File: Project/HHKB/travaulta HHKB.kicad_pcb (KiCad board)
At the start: 4 copper layers, 209.7 x 76.4 mm, 107 parts, among them J1 ARGB, SW1 EC_SW, SW10 EC_SW, SW11 EC_SW, SW12 EC_SW, SW13 EC_SW, SW14 EC_SW, SW15 EC_SW, SW16 EC_SW, SW17 EC_SW, SW18 EC_SW, SW19 EC_SW, SW2 EC_SW, SW20 EC_SW, SW21 EC_SW, SW22 EC_SW, SW23 EC_SW, SW24 EC_SW, SW25 EC_SW, SW26 EC_SW, SW27 EC_SW, SW28 EC_SW, SW29 EC_SW, SW3 EC_SW, SW30 EC_SW, SW31 EC_SW, SW32 EC_SW, SW33 EC_SW, SW34 EC_SW, SW35 EC_SW, SW36 EC_SW, SW37 EC_SW, SW38 BOOT0, SW4 EC_SW, SW5 EC_SW, SW6 EC_SW, SW7 EC_SW, SW8 EC_SW, SW9 EC_SW, U1 STM32F401CBUx, U2 XC6206PxxxMR, U3 74HC4051, U4 74HC4051, U5 OPA350, Y1 8 MHz

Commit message: backup
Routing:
- net GND: track 37.7 -> 45.2 mm, vias 325 -> 321
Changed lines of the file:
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@@
   (via (at 195.012249 65.997905) (size 0.8) (drill 0.4) (layers "F.Cu" "B.Cu") (free) (net 1))
   (via (at 120.888576 104.225245) (size 0.8) (drill 0.4) (layers "F.Cu" "B.Cu") (free) (net 1))
-  (via (at 153.288724 110.807639) (size 0.8) (drill 0.4) (layers "F.Cu" "B.Cu") (net 1))
   (via (at 63.221009 85.070745) (size 0.8) (drill 0.4) (layers "F.Cu" "B.Cu") (free) (net 1))
   (via (at 211.90546 101.6) (size 0.8) (drill 0.4) (layers "F.Cu" "B.Cu") (free) (net 1))
@@
   (via (at 87.3125 63.5) (size 0.8) (drill 0.4) (layers "F.Cu" "B.Cu") (free) (net 1))
   (via (at 104.775 68.278054) (size 0.8) (drill 0.4) (layers "F.Cu" "B.Cu") (free) (net 1))
-  (via (at 150.5501 110.815963) (size 0.8) (drill 0.4) (layers "F.Cu" "B.Cu") (net 1))
   (via (at 136.558834 65.953835) (size 0.8) (drill 0.4) (layers "F.Cu" "B.Cu") (free) (net 1))
   (via (at 227.965 76.2) (size 0.8) (drill 0.4) (layers "F.Cu" "B.Cu") (net 1))
@@
   (via (at 139.953601 68.350091) (size 0.8) (drill 0.4) (layers "F.Cu" "B.Cu") (free) (net 1))
   (via (at 228.6 98.425) (size 0.8) (drill 0.4) (layers "F.Cu" "B.Cu") (net 1))
-  (via (at 153.346 115.062) (size 0.8) (drill 0.4) (layers "F.Cu" "B.Cu") (net 1))
   (via (at 87.653038 51.101306) (size 0.8) (drill 0.4) (layers "F.Cu" "B.Cu") (net 1))
   (via (at 84.074 69.85) (size 0.8) (drill 0.4) (layers "F.Cu" "B.Cu") (free) (net 1))
   (via (at 177.165 119.0625) (size 0.8) (drill 0.4) (layers "F.Cu" "B.Cu") (net 1))
-  (via (at 150.425 115.062) (size 0.8) (drill 0.4) (layers "F.Cu" "B.Cu") (net 1))
   (segment (start 85.75 53.624) (end 86.81 53.624) (width 0.25) (layer "B.Cu") (net 1))
   (segment (start 157.41 114.683) (end 158.047 114.683) (width 0.25) (layer "B.Cu") (net 1))
@@
   (segment (start 77.43 52.764) (end 77.43 51.094) (width 0.25) (layer "B.Cu") (net 1))
   (segment (start 151.896 116.3405) (end 151.896 113.591) (width 0.25) (layer "B.Cu") (net 1))
-  (segment (start 154.851186 115.15718) (end 154.701186 115.00718) (width 0.25) (layer "B.Cu") (net 1))
   (segment (start 77.43 48.864) (end 75.723 48.864) (width 0.25) (layer "B.Cu") (net 1))
   (segment (start 78.29 53.624) (end 77.43 52.764) (width 0.25) (layer "B.Cu") (net 1))
   (segment (start 149.04 118.491) (end 149.031 118.5) (width 0.25) (layer "B.Cu") (net 1))
+  (segment (start 154.889279 110.592899) (end 154.889279 109.405399) (width 0.25) (layer "B.Cu") (net 1))
   (segment (start 82.903 69.85) (end 84.074 69.85) (width 0.25) (layer "B.Cu") (net 1))
-  (segment (start 154.889279 109.405399) (end 154.889279 110.592899) (width 0.25) (layer "B.Cu") (net 1))
+  (segment (start 152.654 112.828178) (end 154.889279 110.592899) (width 0.25) (layer "B.Cu") (net 1))
   (segment (start 152.646 112.903) (end 152.637137 112.903) (width 0.25) (layer "B.Cu") (net 1))
   (segment (start 89.377 48.864) (end 89.408 48.895) (width 0.25) (layer "B.Cu") (net 1))
   (segment (start 81.28 56.39) (end 81.28 57.277) (width 0.25) (layer "B.Cu") (net 1))
   (segment (start 75.723 48.864) (end 75.692 48.895) (width 0.25) (layer "B.Cu") (net 1))
+  (segment (start 154.90818 115.15718) (end 155.575 115.15718) (width 0.25) (layer "B.Cu") (net 1))
   (segment (start 84.201 56.35625) (end 84.201 57.283328) (width 0.25) (layer "B.Cu") (net 1))
-  (segment (start 150.4001 110.665963) (end 150.5501 110.815963) (width 0.25) (layer "B.Cu") (net 1))
   (segment (start 77.43 51.094) (end 77.47 51.054) (width 0.25) (layer "B.Cu") (net 1))
   (segment (start 151.896 116.3405) (end 151.896 118.233) (width 0.25) (layer "B.Cu") (net 1))
@@
   (segment (start 87.67 52.764) (end 87.67 51.118268) (width 0.25) (layer "B.Cu") (net 1))
   (segment (start 158.299 115.635994) (end 158.271 115.663994) (width 0.25) (layer "B.Cu") (net 1))
-  (segment (start 150.5501 110.815963) (end 150.387137 110.653) (width 0.25) (layer "B.Cu") (net 1))
   (segment (start 77.43 51.094) (end 77.43 48.864) (width 0.25) (layer "B.Cu") (net 1))
-  (segment (start 156.038686 115.15718) (end 154.851186 115.15718) (width 0.25) (layer "B.Cu") (net 1))
+  (segment (start 152.654 112.903) (end 154.90818 115.15718) (width 0.25) (layer "B.Cu") (net 1))
   (segment (start 87.67 51.084344) (end 87.67 48.864) (width 0.25) (layer "B.Cu") (net 1))
   (segment (start 151.896 118.233) (end 151.638 118.491) (width 0.25) (layer "B.Cu") (net 1))
-  (segment (start 154.889279 110.592899) (end 154.739279 110.742899) (width 0.25) (layer "B.Cu") (net 1))
+  (segment (start 152.654 112.903) (end 152.654 112.828178) (width 0.25) (layer "B.Cu") (net 1))
+  (segment (start 152.654 112.903) (end 150.404 110.653) (width 0.25) (layer "B.Cu") (net 1))
   (segment (start 151.638 118.491) (end 149.04 118.491) (width 0.25) (layer "B.Cu") (net 1))
   (segment (start 158.299 114.935) (end 158.047 114.683) (width 0.25) (layer "B.Cu") (net 1))
-  (segment (start 149.2126 110.665963) (end 150.4001 110.665963) (width 0.25) (layer "B.Cu") (net 1))
+  (segment (start 156.038686 115.15718) (end 155.575 115.15718) (width 0.25) (layer "B.Cu") (net 1))
   (segment (start 84.201 57.283328) (end 84.198075 57.286253) (width 0.25) (layer "B.Cu") (net 1))
-  (segment (start 150.387137 110.653) (end 149.2165 110.653) (width 0.25) (layer "B.Cu") (net 1))
+  (segment (start 150.404 110.653) (end 149.2165 110.653) (width 0.25) (layer "B.Cu") (net 1))
   (segment (start 153.396 109.4575) (end 153.404 109.4655) (width 0.2) (layer "B.Cu") (net 2))
   (segment (start 81.8 54.474) (end 82.063 54.737) (width 0.2) (layer "B.Cu") (net 2))

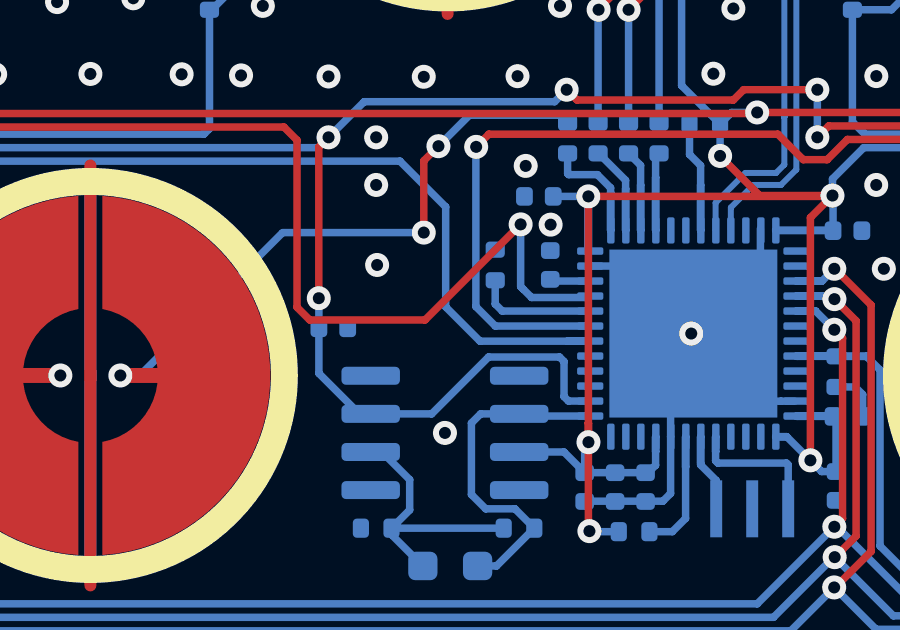
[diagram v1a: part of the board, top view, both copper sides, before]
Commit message: changed rgb pin on HHKB&WKL for better compatibility
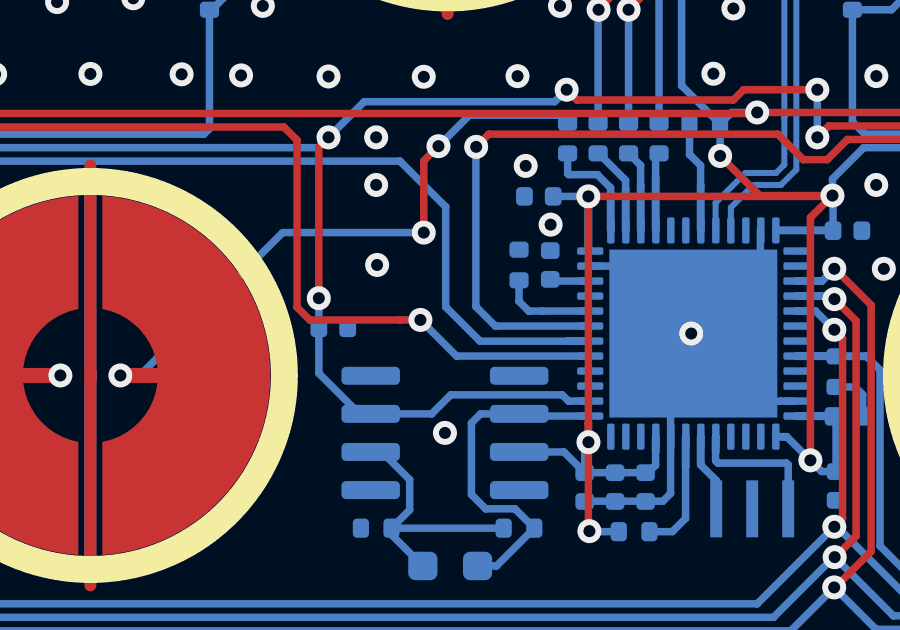
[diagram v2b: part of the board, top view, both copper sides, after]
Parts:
- moved R7 0.79 mm to (146.8, 110.6)
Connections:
- U1 pad 17: unconnected-(U1-PA7-Pad17) -> RGB
- U1 pad 21: RGB -> unconnected-(U1-PB10-Pad21)
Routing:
- net RGB: track 100.3 -> 97.2 mm
- net APLEX_OUT_PIN_0: track 140.6 -> 138.9 mm
- net BOOT1: track 4.06 -> 3.44 mm

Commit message: fresh gerbers for HHKB WKL
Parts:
- removed the G*** at (250.8, 76.2)
- added G***: LOGO, LOGO, B.Cu at (250.8, 82.5)
- added G***: LOGO, LOGO, B.Cu at (246.9, 73.8)
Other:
- board text added: "HHKB"
- board text added: "by Calvin0563"
- board text removed: "by Calvin0563 for mechvault's vault35"
